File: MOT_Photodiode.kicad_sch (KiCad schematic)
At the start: 16 parts, among them J1 Supply, J2 output, J3 photodiode, U1 LT3032-12, U2 ADA4898-1YRDZ

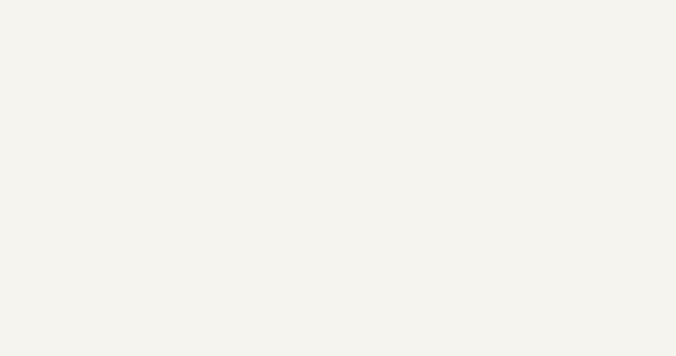
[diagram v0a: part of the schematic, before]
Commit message: Added logos
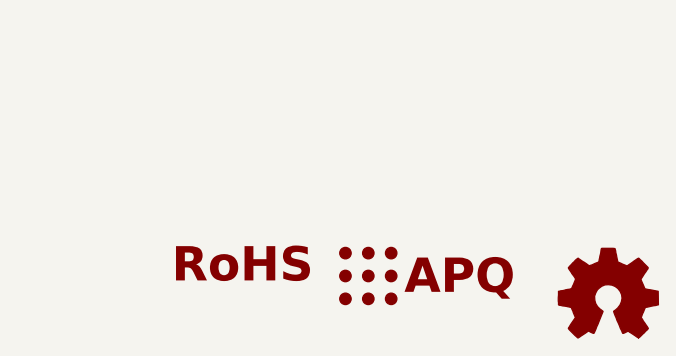
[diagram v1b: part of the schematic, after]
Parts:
- added SYM1: Logo_Open_Hardware_Small, Symbol:OSHW-Logo_7.5x8mm_SilkScreen, symbol Graphic:Logo_Open_Hardware_Small
- added SYM2: Logo_APQ, custom_footprints_project:APQ-Logo_small, symbol Custom_logos:Logo_APQ
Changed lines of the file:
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@@
+	)
+	(symbol
+		(lib_id "Graphic:Logo_Open_Hardware_Small")
+		(at 276.86 172.72 0)
+		(unit 1)
+		(exclude_from_sim yes)
+		(in_bom no)
+		(on_board yes)
+		(dnp no)
+		(fields_autoplaced yes)
+		(property "Reference" "SYM1"
+			(at 276.86 165.735 0)
+			(effects
+				(font
+					(size 1.27 1.27)
+				)
+				(hide yes)
+			)
+		)
+		(property "Value" "Logo_Open_Hardware_Small"
+			(at 276.86 178.435 0)
+			(effects
+				(font
+					(size 1.27 1.27)
+				)
+				(hide yes)
+			)
+		)
+		(property "Footprint" "Symbol:OSHW-Logo_7.5x8mm_SilkScreen"
+			(at 276.86 172.72 0)
+			(effects
+				(font
+					(size 1.27 1.27)
+				)
+				(hide yes)
+			)
+		)
+		(property "Datasheet" "~"
+			(at 276.86 172.72 0)
+			(effects
+				(font
+					(size 1.27 1.27)
+				)
+				(hide yes)
+			)
+		)
+		(property "Description" "Open Hardware logo, small"
+			(at 276.86 172.72 0)
+			(effects
+				(font
+					(size 1.27 1.27)
+				)
+				(hide yes)
+			)
+		)
+		(instances
+			(project ""
+				(path "/a0517d20-38d0-4fc0-8a16-4b6ef5eb9257"
+					(reference "SYM1")
+					(unit 1)
+				)
+			)
+		)
 	)
 	(symbol
@@
 				(path "/a0517d20-38d0-4fc0-8a16-4b6ef5eb9257"
 					(reference "#FLG02")
+					(unit 1)
+				)
+			)
+		)
+	)
+	(symbol
+		(lib_id "Custom_logos:Logo_APQ")
+		(at 256.54 170.18 0)
+		(unit 1)
+		(exclude_from_sim yes)
+		(in_bom no)
+		(on_board yes)
+		(dnp no)
+		(fields_autoplaced yes)
+		(property "Reference" "SYM2"
+			(at 256.54 163.83 0)
+			(effects
+				(font
+					(size 1.27 1.27)
+				)
+				(hide yes)
+			)
+		)
+		(property "Value" "Logo_APQ"
+			(at 256.54 176.53 0)
+			(effects
+				(font
+					(size 1.27 1.27)
+				)
+				(hide yes)
+			)
+		)
+		(property "Footprint" "custom_footprints_project:APQ-Logo_small"
+			(at 250.19 170.18 0)
+			(effects
+				(font
+					(size 1.27 1.27)
+				)
+				(hide yes)
+			)
+		)
+		(property "Datasheet" "~"
+			(at 256.54 170.18 0)
+			(effects
+				(font
+					(size 1.27 1.27)
+				)
+				(hide yes)
+			)
+		)
+		(property "Description" "Atoms - Photons - Quanta"
+			(at 256.54 170.18 0)
+			(effects
+				(font
+					(size 1.27 1.27)
+				)
+				(hide yes)
+			)
+		)
+		(instances
+			(project ""
+				(path "/a0517d20-38d0-4fc0-8a16-4b6ef5eb9257"
+					(reference "SYM2")
 					(unit 1)
 				)
@@
 					(unit 1)
 				)
+			)
+		)
+	)
+	(symbol
+		(lib_id "Custom_logos:SYM_RoHS")
+		(at 236.22 168.91 0)
+		(unit 1)
+		(exclude_from_sim yes)
+		(in_bom no)
+		(on_board no)
+		(dnp no)
+		(fields_autoplaced yes)
+		(property "Reference" "#SYM3"
+			(at 236.22 165.1 0)
+			(effects
+				(font
+					(size 1.27 1.27)
+				)
+				(hide yes)
+			)
+		)
+		(property "Value" "SYM_RoHS"
+			(at 236.22 172.72 0)
+			(effects
+				(font
+					(size 1.27 1.27)
+				)
+				(hide yes)
+			)
+		)
+		(property "Footprint" ""
+			(at 243.84 168.91 0)
+			(effects
+				(font
+					(size 1.27 1.27)
+				)
+				(hide yes)
+			)
+		)
+		(property "Datasheet" "~"
+			(at 236.22 168.91 0)
+			(effects
+				(font
+					(size 1.27 1.27)
+				)
+				(hide yes)
+			)
+		)
+		(property "Description" "RoHS (Restriction of Hazardous Substances Directive) logo"
+			(at 236.22 168.91 0)
+			(effects
+				(font
+					(size 1.27 1.27)
+				)
+				(hide yes)
+			)
+		)
+		(instances
+			(project ""
+				(path "/a0517d20-38d0-4fc0-8a16-4b6ef5eb9257"
+					(reference "#SYM3")
+					(unit 1)
+				)

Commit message: Added BOM
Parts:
- C1, C2, C5, C6: MFN (none) -> Murata; PN (none) -> GCM32EL8EH106KA07L; RoHS (none) -> Yes; Temperature (none) -> Tstorage = –55 °C to 150 °C
- C3, C4: MFN (none) -> TDK; PN (none) -> CGA3E2C0G1H103J080AE; RoHS (none) -> Yes; Temperature (none) -> Tstorage = –55 °C to 125 °C
- C8: MFN (none) -> TDK; PN (none) -> CGA3E2C0G1H331J080AA; RoHS (none) -> Yes; Temperature (none) -> Tstorage = –55 °C to 125 °C
- J1: MFN (none) -> Amphenol; PN (none) -> 54101-T0503LF; RoHS (none) -> Yes; Temperature (none) -> Tstorage = –65 °C to 125 °C
- J2: MFN (none) -> TE Connectivity; PN (none) -> CONSMA001-C-G; RoHS (none) -> Yes; Temperature (none) -> Tstorage = –65°C to +165°C
- J3: MFN (none) -> Amphenol; PN (none) -> 54101-T0802LF; RoHS (none) -> Yes; Temperature (none) -> Tstorage = –65 °C to 125 °C
- R3: MFN (none) -> Susumu; PN (none) -> RG1608P-2671-B-T5; RoHS (none) -> Yes; Temperature (none) -> Tstorage = –55°C to +155°C
- R4: value 49.9 -> 49.9R; MFN (none) -> Yageo; PN (none) -> AC1210FR-0749R9L; RoHS (none) -> By exemption; Temperature (none) -> Tstorage = –55°C to +155°C
- U1: MFN (none) -> Analog Devices; PN (none) -> LT3032IDE-12#PBF; RoHS (none) -> Yes; Temperature (none) -> Tstorage = –40°C to 125°C
- U2: MFN (none) -> Analog Devices; PN (none) -> ADA4898-1YRDZ; RoHS (none) -> Yes; Temperature (none) -> Tstorage = –65°C to +150°C

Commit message: Update/kicad9 (#2)
* Update files to KiCad 9 incl. footprint updates

* Bump CI to KiCad 9

* Refilled copper pour

* Bump version to 1.1.1
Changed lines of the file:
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@@
 (kicad_sch
-	(version 20231120)
+	(version 20250114)
 	(generator "eeschema")
-	(generator_version "8.0")
+	(generator_version "9.0")
 	(paper "A4")
 	(title_block
 		(title "MOT Photodiode")
-		(date "2025-02-27")
-		(rev "1.1.0")
+		(date "2025-06-24")
+		(rev "1.1.1")
 		(company "Atoms Photons Quanta")
 		(comment 1 "and Tilman Preuschoff")
@@
 		(comment 3 "Licensed under CERN OHL v.1.2")
 	)
+	(text "-"
+		(exclude_from_sim no)
+		(at 121.92 71.12 0)
+		(effects
+			(font
+				(size 1.524 1.524)
+			)
+			(justify left bottom)
+		)
+	)
+	(text "+"
+		(exclude_from_sim no)
+		(at 121.92 81.28 0)
+		(effects
+			(font
+				(size 1.524 1.524)
+			)
+			(justify left bottom)
+		)
+	)
 	(junction
 		(at 162.56 77.47)
@@
 		)
 	)
-	(text "-"
-		(exclude_from_sim no)
-		(at 121.92 71.12 0)
-		(effects
-			(font
-				(size 1.524 1.524)
-			)
-			(justify left bottom)
-		)
-	)
-	(text "+"
-		(exclude_from_sim no)
-		(at 121.92 81.28 0)
-		(effects
-			(font
-				(size 1.524 1.524)
-			)
-			(justify left bottom)
-		)
-	)
 	(global_label "V-"
 		(shape input)
@@
 			)
 		)
-		(property "Description" ""
+		(property "Description" "Resistor, small symbol"
 			(at 151.13 53.34 0)
 			(effects
@@
 			)
 		)
-		(property "Description" ""
+		(property "Description" "Resistor, small symbol"
 			(at 175.26 77.47 0)
 			(effects
@@
 		)
 	)
+	(embedded_fonts no)
 )
